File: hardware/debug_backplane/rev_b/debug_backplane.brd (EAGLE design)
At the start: 177.8 x 177.8 mm, 329 parts, among them J1 BACKPLANE_CONTROLLER_MODULE_D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, J11 PJ-102AH, J2 BACKPLANE_GENERIC_MODULE_DEBUG, J3 BACKPLANE_GENERIC_MODULE_DEBUG, J4 MICRO_USB_B_HIROSE_ZX62R-B-5P, J5 MICRO_USB_B_HIROSE_ZX62R-B-5P, J6 MICRO_USB_B_HIROSE_ZX62R-B-5P, J7 MICRO_USB_B_HIROSE_ZX62R-B-5P, J8 MICRO_USB_B_HIROSE_ZX62R-B-5P, J9 MICRO_USB_B_HIROSE_ZX62R-B-5P, Q1 DMN32D2LDF, Q2 MOSFET-NCHANNELSMD, Q3 MOSFET-NCHANNELSMD, Q4 MOSFET-NCHANNELSMD, Q5 MOSFET-NCHANNELSMD, Q6 MOSFET-NCHANNELSMD, Q7 MOSFET-NCHANNELSMD, Q8 MOSFET-NCHANNELSMD, Q9 MOSFET-NCHANNELSMD, U1 FT232RQ, U10 LTC2941, U11 LTC2941, U12 MAX8887EZK33+T, U13 MCP23008QFN, U14 MCP23008QFN, U15 PCA9544AQFN-N20, U16 SAM4LC8AA, U17 SN74LVC2T45, U18 SN74LVC2T45, U19 SN74LVC2T45, U2 FT232RQ, U20 SN74LVC2T45, U21 TS3USB30E, U22 TS3USB30E, U23 TS3USB30E, U24 TUSB2077A, U3 FT232RQ, U4 FT232RQ, U5 FT232RQ, U6 FXMA2102, U7 FXMA2102, U8 LTC2941, U9 LTC2941, X1 16MHz, Y1 ABMM

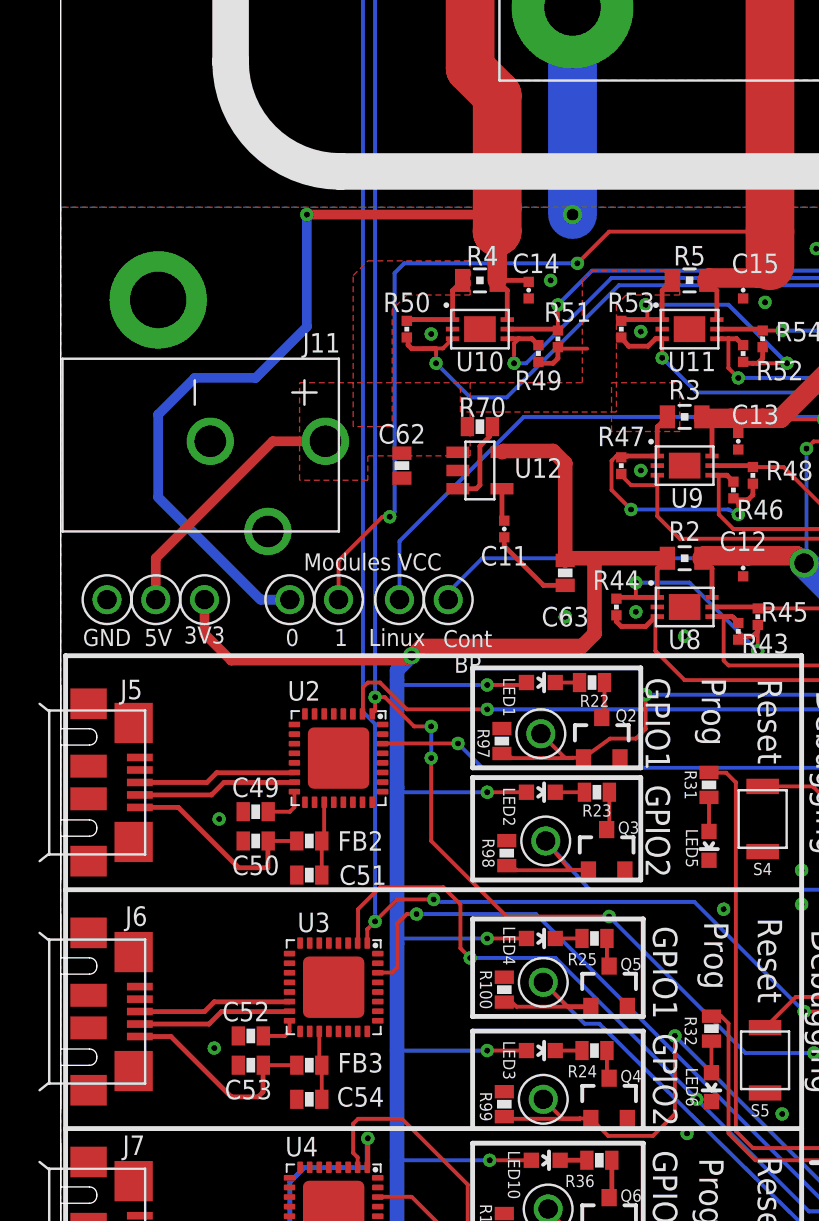
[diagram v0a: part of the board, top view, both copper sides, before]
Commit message: added overvoltage protection circuit
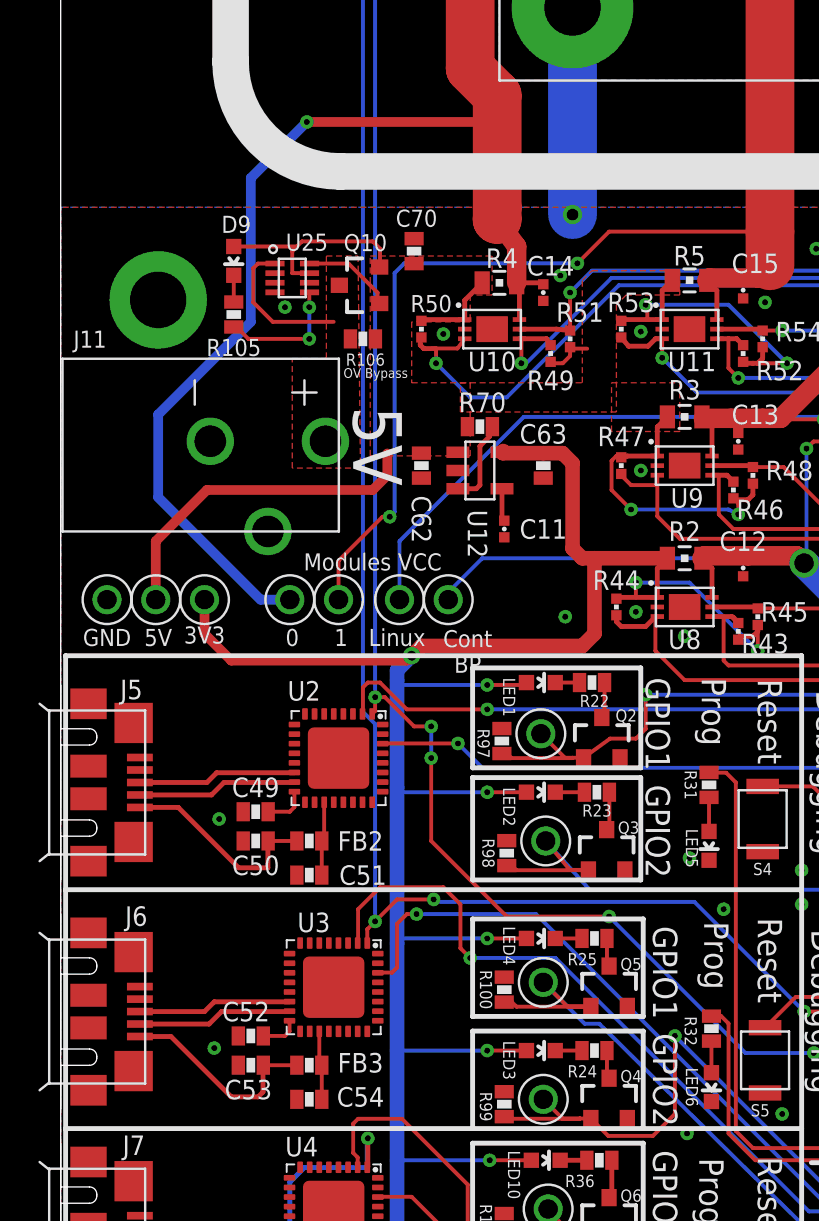
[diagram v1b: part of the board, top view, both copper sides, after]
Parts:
- added C70: 4.7uF, passives:0603_CAP
- added D9: LED0603, leds:LED-0603
- added Q10: MOSFET-NCHANNELSMD, fets:SOT23-3
- added R105: 1kΩ, passives:0603-RES
- added R106: 0Ω - DNP, passives:0603-RES
- added U25: LTC4360, chips:SC70-8
- R71: value 10kΩ -> 10kΩ - DNP
- moved C63 5.70 mm to (25.1, 80.3)
- moved R4 1.02 mm to (22.9, 89.8)
- moved C62 1.02 mm to (18.8, 80.3)
- moved C14 0.77 mm to (25.1, 89.3)
- moved R50 0.76 mm to (18.8, 87.4)
- moved R49 0.64 mm to (25.5, 86.1)
- moved R51 0.63 mm to (26.5, 86.9)
- moved U10 0.63 mm to (22.5, 87.4)
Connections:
- new net N$82: J11.1, Q10.3, R106.2, U25.1
- new net N$83: Q10.1, U25.8
- new net N$84: R105.1, U25.5
- new net N$85: D9.C, R105.2
- net 5V: now also C70.1, D9.A, Q10.2, R106.1, U25.7; no longer J11.1
- net GND: now also C70.2, U25.2, U25.3, U25.4, U25.6
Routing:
- net 5V: track 55.2 -> 69.8 mm
- net N$82: track 0.00 -> 7.62 mm
- net N$84: track 0.00 -> 6.62 mm, vias 0 -> 2
- net MOD0_5V_METERED: track 129.6 -> 135.8 mm
- net N$83: track 0.00 -> 4.79 mm
- net GND: track 614.6 -> 610.1 mm, vias 173 -> 174
- net N$85: track 0.00 -> 1.39 mm
- added copper zone on layer 1, net N$82
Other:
- board text added: "OV Bypass"

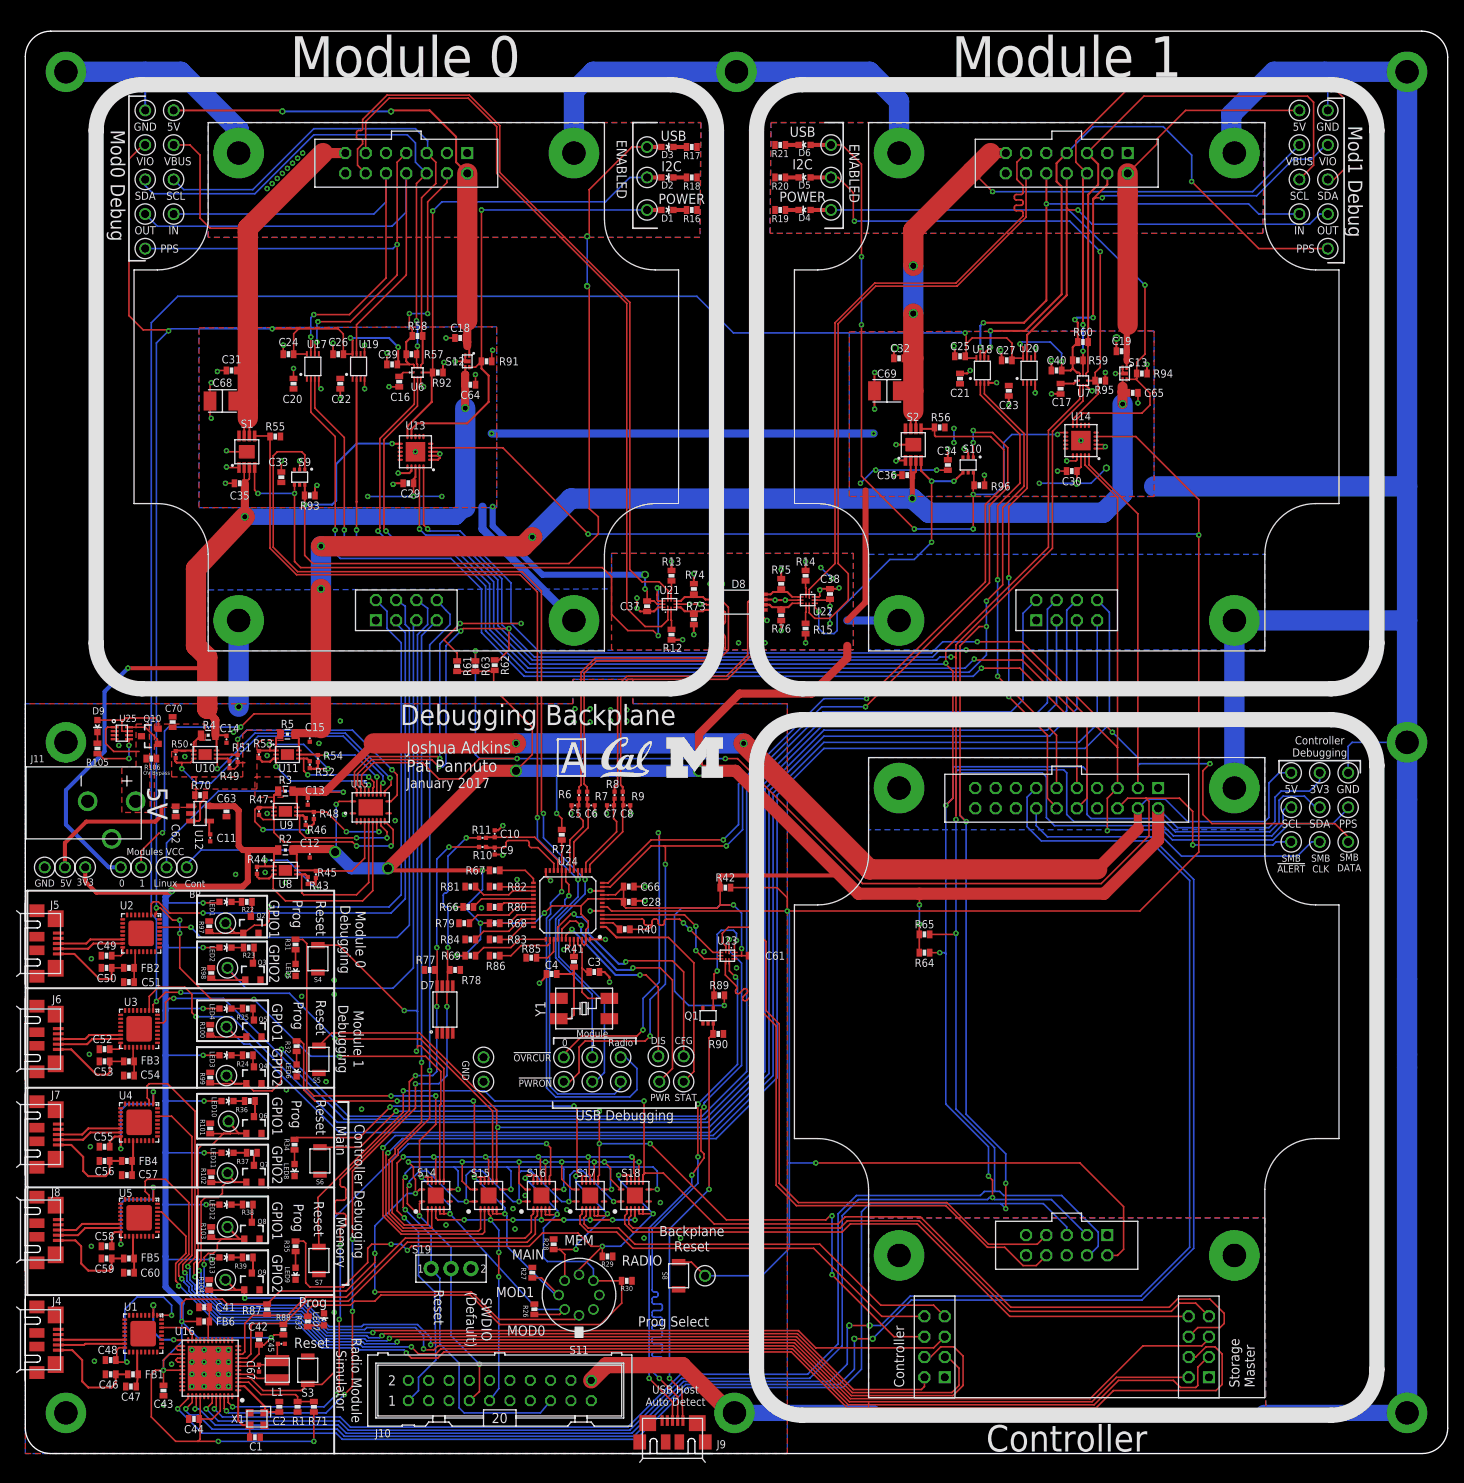
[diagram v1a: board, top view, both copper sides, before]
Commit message: fixed up the header and debug info
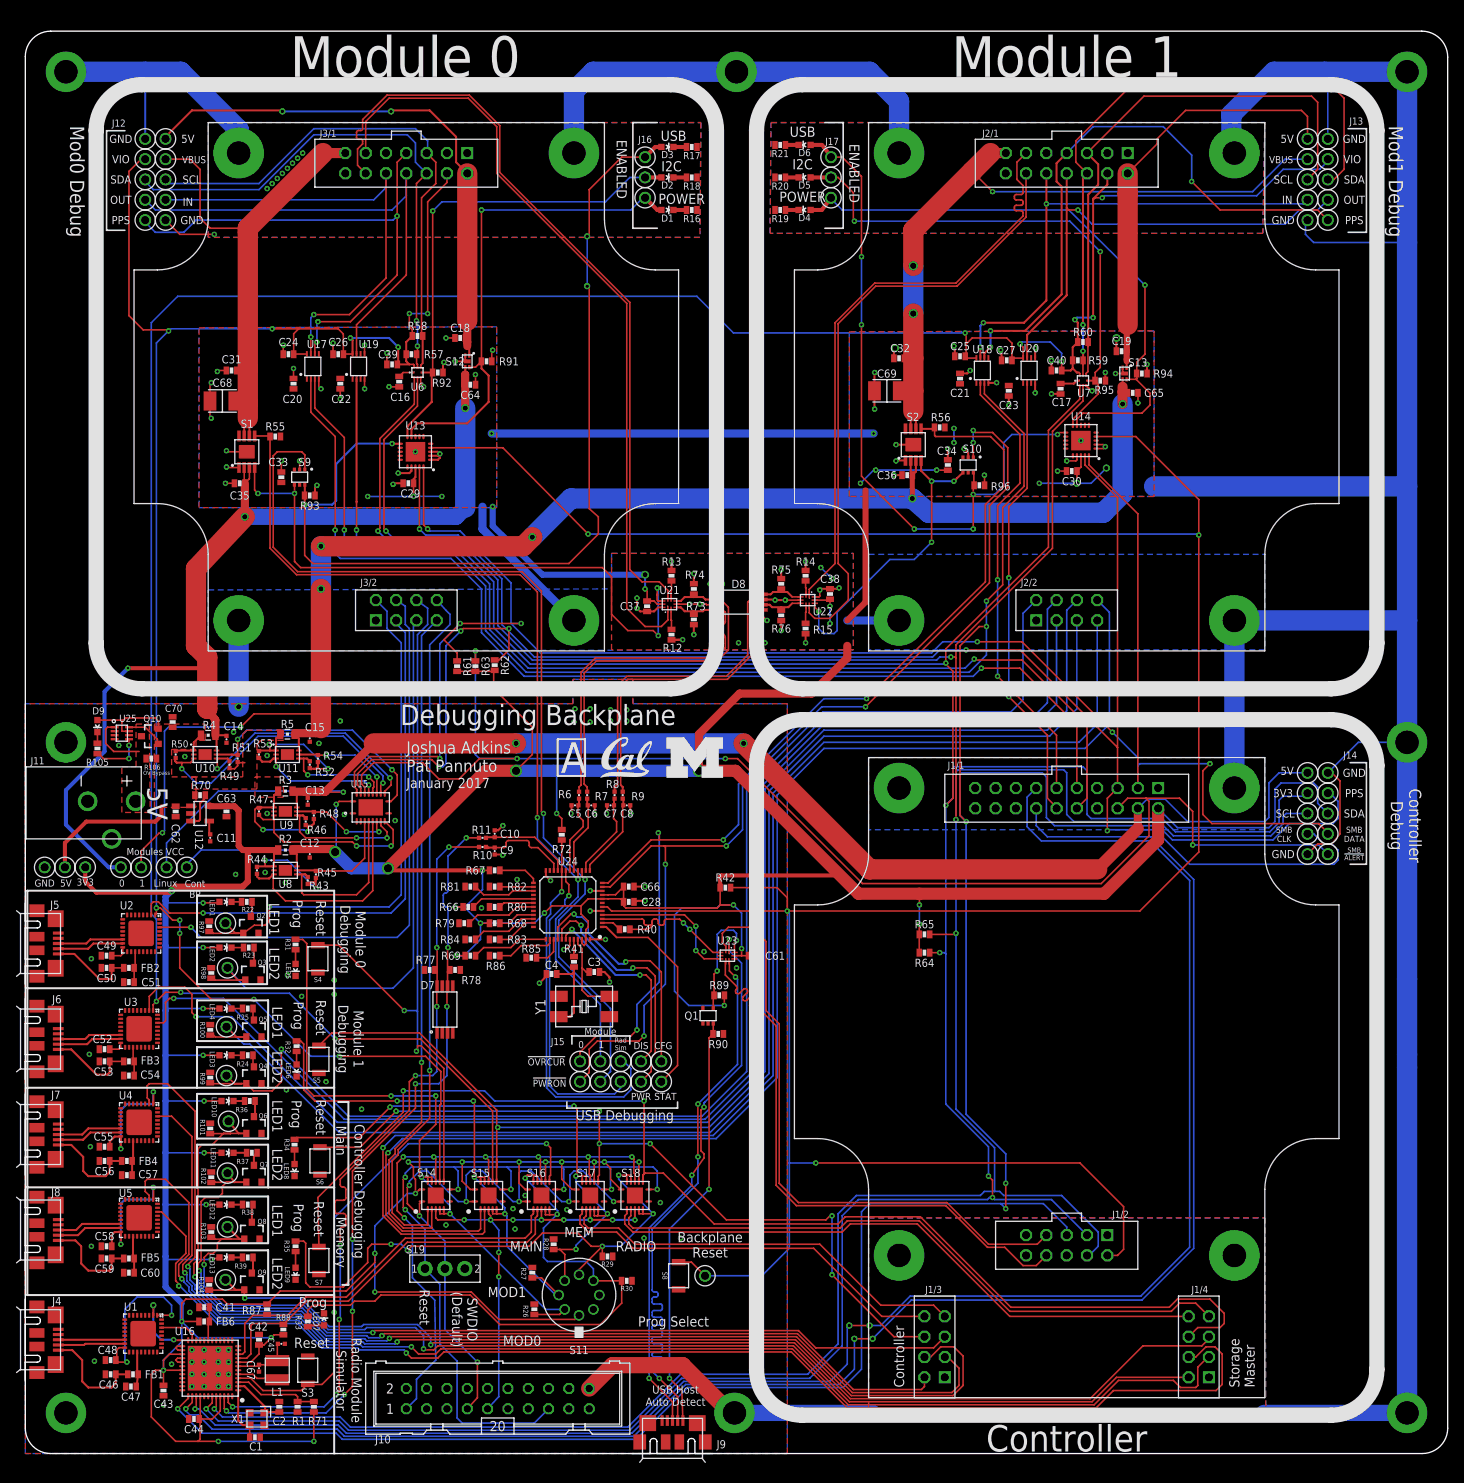
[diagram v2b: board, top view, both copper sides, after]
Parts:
- added TP19: TEST_POINT_0.040IN, headers:TESTPOINT_0.040IN
- moved TP51 149.0 mm to (160.3, 154.2)
- moved TP25 111.9 mm to (17.5, 154.2)
- moved TP24 5.18 mm to (162.8, 80.0)
- moved TP3 4.82 mm to (162.8, 74.9)
- moved TP57 3.70 mm to (17.5, 164.3)
- moved TP58 3.70 mm to (160.3, 164.3)
- moved TP27 3.56 mm to (162.8, 164.3)
- moved TP54 3.56 mm to (15.0, 164.3)
- moved TP46 3.56 mm to (15.0, 154.2)
- moved TP47 3.56 mm to (162.8, 154.2)
- moved TP10 3.10 mm to (162.8, 82.5)
- moved TP28 2.87 mm to (79.5, 49.0)
- moved TP31 2.79 mm to (79.5, 46.5)
- moved TP1 2.74 mm to (162.8, 77.5)
- moved TP11 2.54 mm to (162.8, 85.1)
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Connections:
- net GND: now also TP19.TESTPOINT
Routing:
- net GND: track 610.1 -> 654.1 mm, vias 174 -> 175
- net SMBCLK: track 231.9 -> 240.0 mm
- net !SMBALERT: track 164.1 -> 169.0 mm
- net MOD1_5V: track 50.4 -> 54.5 mm
- net SMBDATA: track 243.9 -> 240.6 mm
- net VCC_BACKPLANE: track 523.8 -> 527.0 mm
- net MOD0_5V: track 67.5 -> 70.2 mm
- net HUB_!PWRON1: track 133.4 -> 130.8 mm
- net HUB_CFG: track 32.5 -> 30.4 mm
- net MOD0_OUT: track 64.0 -> 61.9 mm
- net VCC_LINUX: track 179.4 -> 181.4 mm
- net USB_SUSPEND_STATUS: track 28.7 -> 26.7 mm
- net MOD_SDA: track 414.4 -> 412.4 mm
- net PPS: track 433.5 -> 435.4 mm
- net HUB_!OVRCUR1: track 134.0 -> 132.2 mm
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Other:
- board text added: "Controller Debug"
- board text added: "J1/1"
- board text added: "J1/2"
- board text added: "J1/3"
- board text added: "J1/4"
- board text added: "J12"
- board text added: "J13"
- board text added: "J14"
- board text added: "J15"
- board text added: "J16"
- board text added: "J17"
- board text added: "J2/1"
- board text added: "J2/2"
- board text added: "J3/1"
- board text added: "J3/2"
- board text added: "LED1"
- board text added: "LED2"
- board text added: "Rad Sim"
- board text removed: "GPIO1"
- board text removed: "GPIO2"
- board text removed: "Radio"
